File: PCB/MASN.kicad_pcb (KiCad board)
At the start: 2 copper layers, 35 x 35 mm, 40 parts, among them J1 USB4500-03-0-A, J2 73412-0110, J3 5044490207, J4 SIM8051-6-0-14-00, J6 5044490507, J7 5044490207, J8 73412-0110, J9 5051100792, SW1 PTS636 SM43 SMTR LFS, U1 STM32L452RET6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

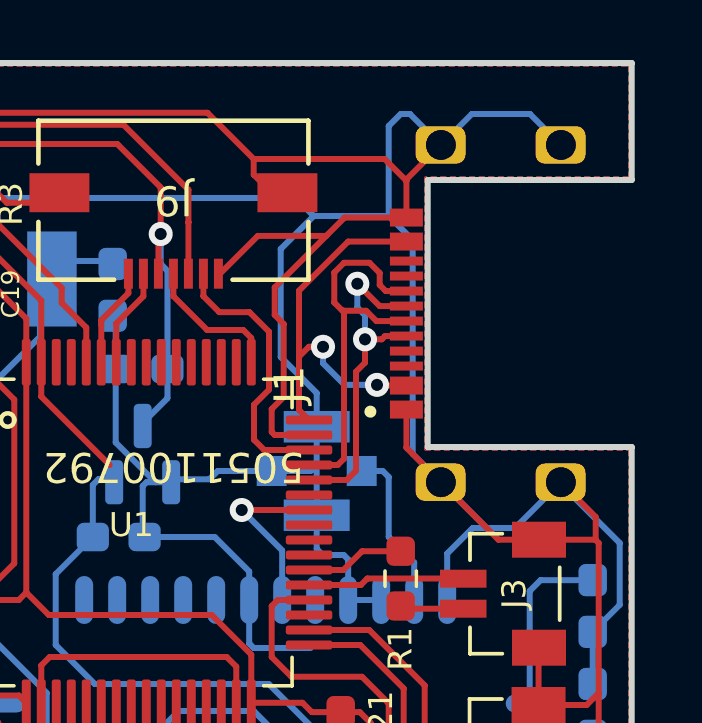
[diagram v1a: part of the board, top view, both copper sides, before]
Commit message: Delta-coding, automatic IMEI and timestamp working (1 s samples)
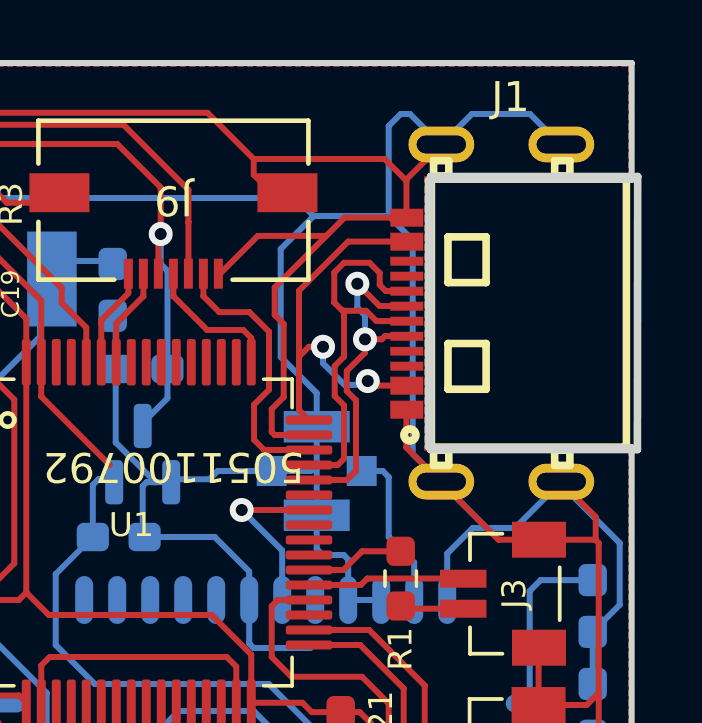
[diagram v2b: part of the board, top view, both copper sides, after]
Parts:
- J1: value USB4500-03-0-A -> USB-310CA; footprint USB4500-03-0-A_REVA:GCT_USB4500-03-0-A_REVA -> Customs:USB-C-SMD_20P-P0.50-L6.5-W11.2
- SW1: value PTS636 SM43 SMTR LFS -> PTS636SM43JSMTR LFS
- U3: value MCP1700T-2302E/TT -> MCP1700T-2302E/TT
- moved J1 0.80 mm to (56.7, 110.2), turned to 0 degrees
